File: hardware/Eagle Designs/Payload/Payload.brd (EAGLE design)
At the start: 90.2 x 95.5 mm, 81 parts, among them J1 503763-0591, J2 503763-0591, J3 MOLEX_503763-0491MOLEX_503763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, J4 503763-0691, J5 MOLEX_503763-0291MOLEX_503763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, J6 503763-0691, J7 503763-0691, M1 BSZ100N06LS3, M2 BSZ100N06LS3, M3 BSZ033NE2LS5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

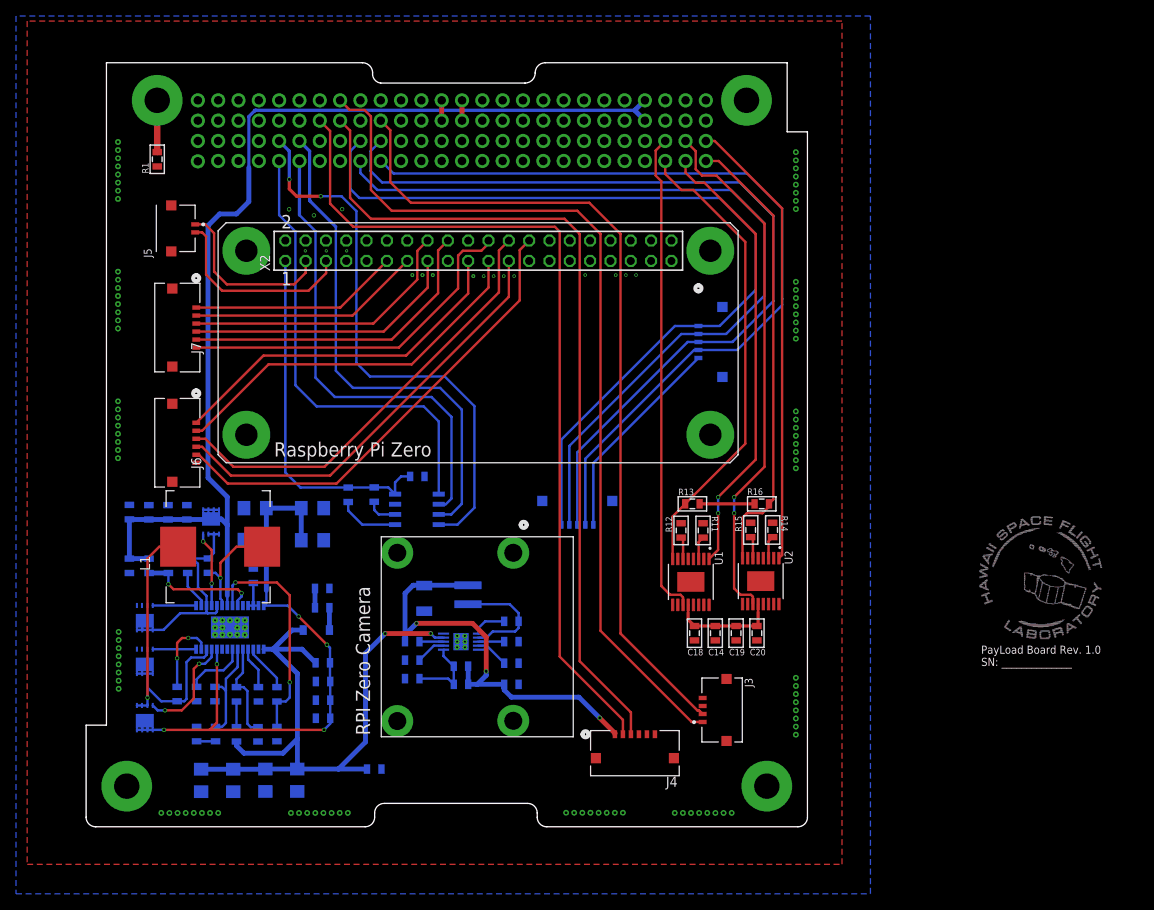
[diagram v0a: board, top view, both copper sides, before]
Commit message: Edited payload board, created payload and bbb obc BOM
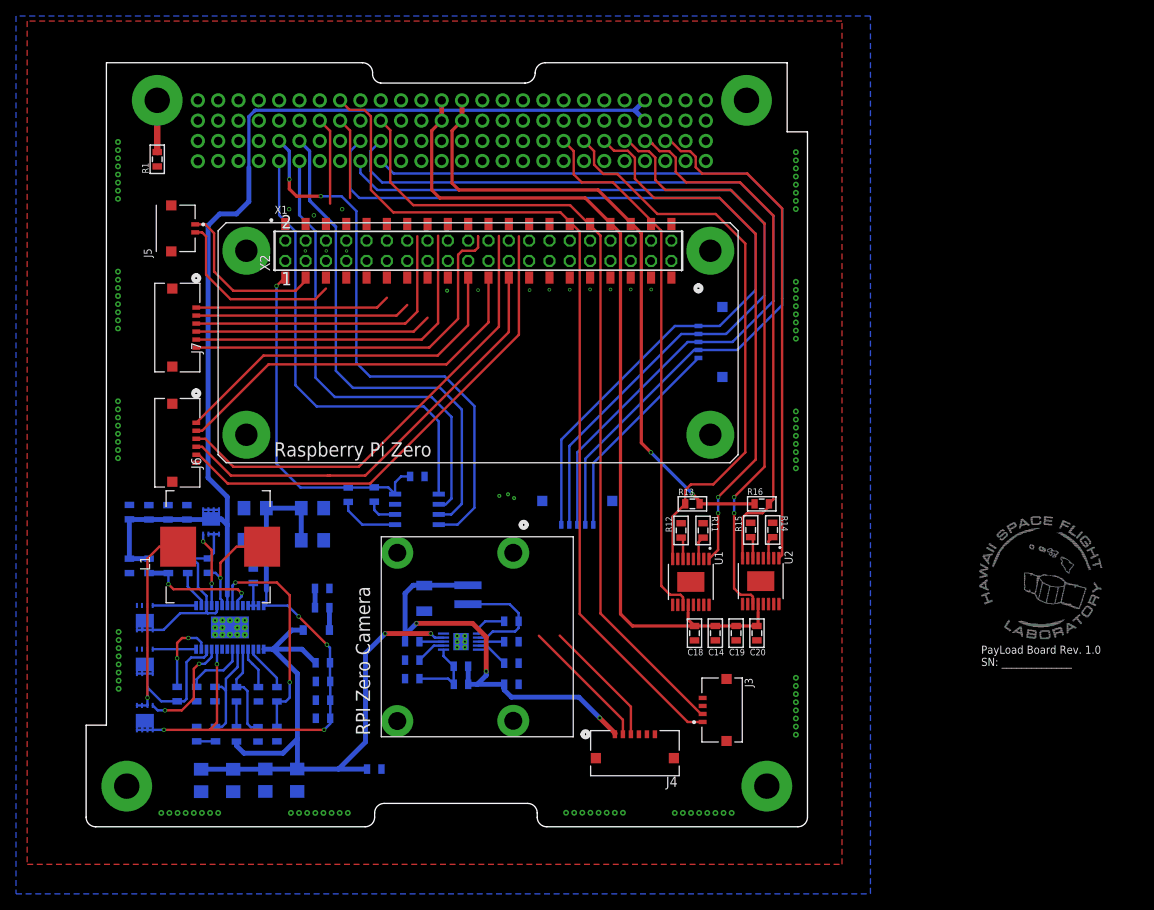
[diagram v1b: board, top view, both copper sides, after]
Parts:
- added X1: C25582-40G-M36-0A, Adafruit - C25582-40G-M36-0A:ADAFRUIT_C25582-40G-M36-0A_0
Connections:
- removed net 3V3: R13.2, R16.2
- removed net 5V: C14.2, C18.2, C19.2, C20.2, U1.12, U2.12
- net +3V3_BUS: now also R13.2, R16.2
- net +3V3_VCC: now also X1.1; no longer X2.1
- net +5V_BUS: now also C14.2, C18.2, C19.2, C20.2, U1.12, U2.12
- net GPIO12: now also X1.32; no longer X2.32
- net GPIO13: now also X1.33; no longer X2.33
- net GPIO16: now also X1.36; no longer X2.36
- net GPIO17: now also X1.11; no longer X2.11
- net GPIO19: now also X1.35; no longer X2.35
- net GPIO20: now also X1.38; no longer X2.38
- net GPIO21: now also X1.40; no longer X2.40
- net GPIO22: now also X1.15; no longer X2.15
- net GPIO23: now also X1.16; no longer X2.16
- net GPIO24: now also X1.18; no longer X2.18
- net GPIO25: now also X1.22; no longer X2.22
- net GPIO26: now also X1.37; no longer X2.37
- net GPIO27: now also X1.13; no longer X2.13
- net GPIO6: now also X1.31; no longer X2.31
- net GPIO_FAULT1: now also H1.1.40; no longer H1.1.47
- net GPIO_FAULT2: now also H1.1.46; no longer H1.1.51
- net GPIO_SLEEP1: now also H1.1.42; no longer H1.1.49
- net GPIO_SLEEP2: now also H1.1.48; no longer H1.1.52
- net GPIO_TRQ1: now also H1.1.38; no longer H1.1.48
- net GPIO_TRQ2: now also H1.1.44; no longer H1.1.50
- net SCL1_I2C: now also X1.5; no longer X2.5
- net SDA1_I2C: now also X1.3; no longer X2.3
- net SPI0_CE0_N: now also X1.24; no longer X2.24
- net SPI0_CE1_N: now also X1.26; no longer X2.26
- net SPI0_MISO: now also X1.21; no longer X2.21
- net SPI0_MOSI: now also X1.19; no longer X2.19
- net SPI0_SCLK: now also X1.23; no longer X2.23
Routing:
- net +5V_BUS: track 2.54 -> 108.6 mm
- net 5V_SW3: track 105.9 -> 26.2 mm
- net 5V_SW2: track 107.2 -> 27.6 mm
- net +3V3_BUS: track 2.54 -> 80.8 mm, vias 0 -> 2
- net 5V: track 13.6 -> 0.00 mm
- net GPIO_FAULT1: track 58.5 -> 71.3 mm
- net GPIO_SLEEP1: track 56.4 -> 68.3 mm
- net GPIO_FAULT2: track 56.8 -> 66.6 mm
- net GPIO_TRQ2: track 66.3 -> 74.3 mm
- net 3V3: track 6.87 -> 0.00 mm
- net GPIO_TRQ1: track 60.7 -> 67.2 mm
- net GPIO_SLEEP2: track 56.9 -> 62.8 mm
- net GPIO22: track 34.5 -> 29.6 mm
- net GPIO23: track 35.3 -> 38.0 mm
- net SPI0_CE0_N: track 55.3 -> 57.9 mm
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
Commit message: Update payload board
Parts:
- added J8, J9: MOLEX_503763-0491MOLEX_503763-0491_0_0, Molex - 503763-0491:MOLEX_503763-0491_0
- moved J3 15.4 mm to (80.0, 30.0), flipped to the bottom, turned to 90 degrees
- moved J4 13.8 mm to (80.0, 16.9), flipped to the bottom, turned to 90 degrees
- moved R11 1.40 mm to (77.1, 38.4)
- moved R12 1.40 mm to (74.4, 38.4)
- moved R14 1.35 mm to (85.9, 38.5)
- moved R15 1.35 mm to (83.1, 38.5)
- moved C18 1.20 mm to (76.0, 23.0)
- moved R16 1.20 mm to (84.5, 41.6)
- moved C14 1.20 mm to (78.6, 23.0)
- moved C19 1.20 mm to (81.2, 23.0)
- moved C20 1.20 mm to (83.9, 23.0)
- moved R13 1.20 mm to (75.8, 41.6)
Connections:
- net 12V_SW1: now also J4.3; no longer J4.1
- net 3V3_SW1: now also J3.1; no longer J3.2
- net 5V_SW3: now also J4.1; no longer J4.3
- net 5V_SW4: now also J3.2; no longer J3.1
- net IN1: now also H1.1.26
- net IN2: now also H1.1.25
- net IN3: now also H1.1.23
- net IN4: now also H1.1.24
- net IN5: now also H1.1.30
- net IN6: now also H1.1.29
- net IN7: now also H1.1.27
- net IN8: now also H1.1.28
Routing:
- net +5V_BUS: track 108.6 -> 18.5 mm
- net 5V_SW2: track 27.6 -> 113.1 mm, vias 0 -> 1
- net 5V_SW3: track 26.2 -> 109.9 mm, vias 0 -> 1
- net IN4: track 0.00 -> 81.8 mm, vias 0 -> 1
- net IN5: track 0.00 -> 80.3 mm, vias 0 -> 1
- net IN1: track 0.00 -> 80.1 mm, vias 0 -> 1
- net IN8: track 0.00 -> 80.0 mm, vias 0 -> 1
- net IN3: track 0.00 -> 74.1 mm, vias 0 -> 1
- net IN6: track 0.00 -> 73.7 mm, vias 0 -> 1
- net IN7: track 0.00 -> 73.1 mm, vias 0 -> 1
- net IN2: track 0.00 -> 72.5 mm, vias 0 -> 1
- net +3V3_BUS: track 80.8 -> 9.41 mm, vias 2 -> 0
- net 3V3_SW1: track 102.4 -> 91.0 mm, vias 0 -> 1
- net 12V_SW1: track 63.4 -> 73.5 mm, vias 3 -> 2
- net 5V_SW4: track 110.9 -> 102.7 mm, vias 0 -> 1
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
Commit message: Update Payload board file
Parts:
- moved C14 3.00 mm to (78.6, 20.0)
- moved C18 3.00 mm to (76.0, 20.0)
- moved C19 3.00 mm to (81.2, 20.0)
- moved C20 3.00 mm to (83.9, 20.0)
- moved U1 2.00 mm to (75.6, 28.6)
- moved U2 2.00 mm to (84.3, 28.7)
- moved J3 1.80 mm to (80.0, 31.8)
- moved J4 0.60 mm to (80.0, 16.4)
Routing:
- net IN1: track 80.1 -> 83.4 mm
- net IN4: track 81.8 -> 85.2 mm
- net IN8: track 80.0 -> 82.5 mm
- net IN5: track 80.3 -> 82.8 mm
- net IN3: track 74.1 -> 76.1 mm
- net GPIO_SLEEP2: track 62.8 -> 64.8 mm
- net IN7: track 73.1 -> 75.1 mm
- net IN6: track 73.7 -> 75.7 mm
- net IN2: track 72.5 -> 74.5 mm
- net GPIO_TRQ2: track 74.3 -> 76.3 mm
- net GPIO_TRQ1: track 68.2 -> 70.2 mm
- net GPIO_SLEEP1: track 68.3 -> 70.3 mm
- net GPIO_FAULT1: track 71.4 -> 73.4 mm
- net +5V_BUS: track 18.5 -> 20.5 mm
- net N$20: track 4.11 -> 6.11 mm
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
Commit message: Payload board changes
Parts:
- moved C14 20.7 mm to (70.4, 39.0), turned to 270 degrees
- moved C19 19.8 mm to (75.6, 39.0), turned to 270 degrees
- moved C20 19.8 mm to (78.3, 39.0), turned to 270 degrees
- moved C18 19.2 mm to (73.0, 39.0), turned to 270 degrees
- moved R11 17.3 mm to (64.0, 27.2), turned to 90 degrees
- moved R13 15.3 mm to (72.0, 26.8), turned to 270 degrees
- moved R14 15.0 mm to (75.9, 27.2), turned to 90 degrees
- moved R16 14.8 mm to (83.9, 26.8), turned to 270 degrees
- moved J6 14.4 mm to (11.4, 62.4)
- moved J7 14.4 mm to (11.4, 48.0)
- moved R12 7.97 mm to (72.0, 30.8), turned to 90 degrees
- moved R15 7.67 mm to (83.9, 30.8), turned to 90 degrees
- moved U1 7.61 mm to (68.0, 29.0), turned to 90 degrees
- moved U2 4.40 mm to (79.9, 28.9), turned to 90 degrees
- moved J3 1.00 mm to (81.0, 31.8)
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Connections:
- net GND: now also J7.6; no longer J6.6
- net GPIO17: now also J6.1; no longer J7.1
- net GPIO22: now also J6.4; no longer J7.4
- net GPIO23: now also J6.3; no longer J7.3
- net GPIO24: now also J6.5; no longer J7.5
- net GPIO25: now also J6.6; no longer J7.6
- net GPIO27: now also J6.2; no longer J7.2
- net SPI0_CE0_N: now also J7.3; no longer J6.3
- net SPI0_CE1_N: now also J7.5; no longer J6.5
- net SPI0_MISO: now also J7.2; no longer J6.2
- net SPI0_MOSI: now also J7.1; no longer J6.1
- net SPI0_SCLK: now also J7.4; no longer J6.4
- net TORQUE_1A: now also J8.1
- net TORQUE_1B: now also J8.2
- net TORQUE_2A: now also J8.4
- net TORQUE_2B: now also J8.3
- net TORQUE_3A: now also J9.1
- net TORQUE_3B: now also J9.2
- net TORQUE_4A: now also J9.4
- net TORQUE_4B: now also J9.3
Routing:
- net IN5: track 82.8 -> 21.8 mm, vias 1 -> 0
- net IN6: track 75.7 -> 19.2 mm, vias 1 -> 0
- net IN4: track 85.2 -> 29.7 mm, vias 1 -> 0
- net IN7: track 75.1 -> 20.3 mm, vias 1 -> 0
- net IN1: track 83.4 -> 29.7 mm, vias 1 -> 0
- net IN8: track 82.5 -> 29.9 mm, vias 1 -> 0
- net IN3: track 76.1 -> 26.7 mm, vias 1 -> 0
- net IN2: track 74.5 -> 26.8 mm, vias 1 -> 0
- net GPIO_SLEEP2: track 64.8 -> 18.9 mm
- net GPIO_SLEEP1: track 70.3 -> 100.8 mm
- net TORQUE_1B: track 0.00 -> 18.8 mm
- net TORQUE_2A: track 0.00 -> 18.8 mm
- net TORQUE_2B: track 0.00 -> 18.7 mm
- net TORQUE_1A: track 0.00 -> 18.7 mm
- net TORQUE_4A: track 0.00 -> 18.5 mm
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
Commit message: Payload board changes
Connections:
- net IN1: now also H1.1.24; no longer H1.1.26
- net IN2: now also H1.1.23; no longer H1.1.25
- net IN3: now also H1.1.25; no longer H1.1.23
- net IN4: now also H1.1.26; no longer H1.1.24
- net IN5: now also H1.1.28; no longer H1.1.30
- net IN6: now also H1.1.27; no longer H1.1.29
- net IN7: now also H1.1.29; no longer H1.1.27
- net IN8: now also H1.1.30; no longer H1.1.28
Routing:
- net +3V3_BUS: track 17.3 -> 119.5 mm, vias 2 -> 3
- net +5V_BUS: track 10.4 -> 100.6 mm, vias 0 -> 1
- net GPIO_SLEEP2: track 18.9 -> 89.9 mm, vias 0 -> 2
- net IN7: track 20.3 -> 73.4 mm, vias 0 -> 1
- net IN5: track 21.8 -> 67.6 mm, vias 0 -> 1
- net IN6: track 19.2 -> 64.4 mm, vias 0 -> 1
- net IN8: track 29.9 -> 68.8 mm, vias 0 -> 1
- net IN1: track 29.7 -> 68.3 mm, vias 0 -> 1
- net IN4: track 29.7 -> 67.9 mm, vias 0 -> 1
- net IN3: track 26.7 -> 64.2 mm, vias 0 -> 1
- net IN2: track 26.8 -> 64.0 mm, vias 0 -> 1
- net GPIO_TRQ1: track 63.3 -> 63.4 mm, vias 0 -> 2
